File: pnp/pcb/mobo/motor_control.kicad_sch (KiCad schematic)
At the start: 0 parts

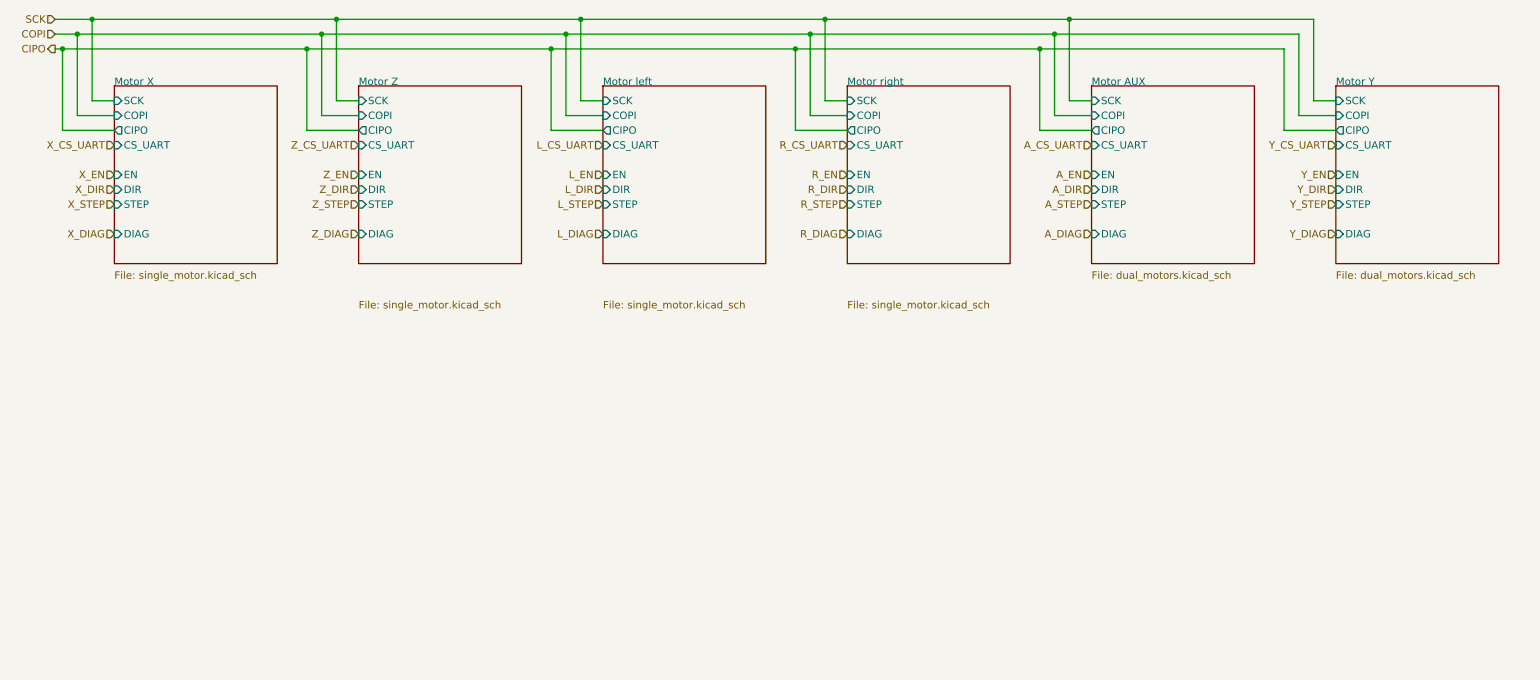
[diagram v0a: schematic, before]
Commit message: Update dual_motors.kicad_sch, mobo.kicad_pcb, mobo.kicad_pro, and 2 more files
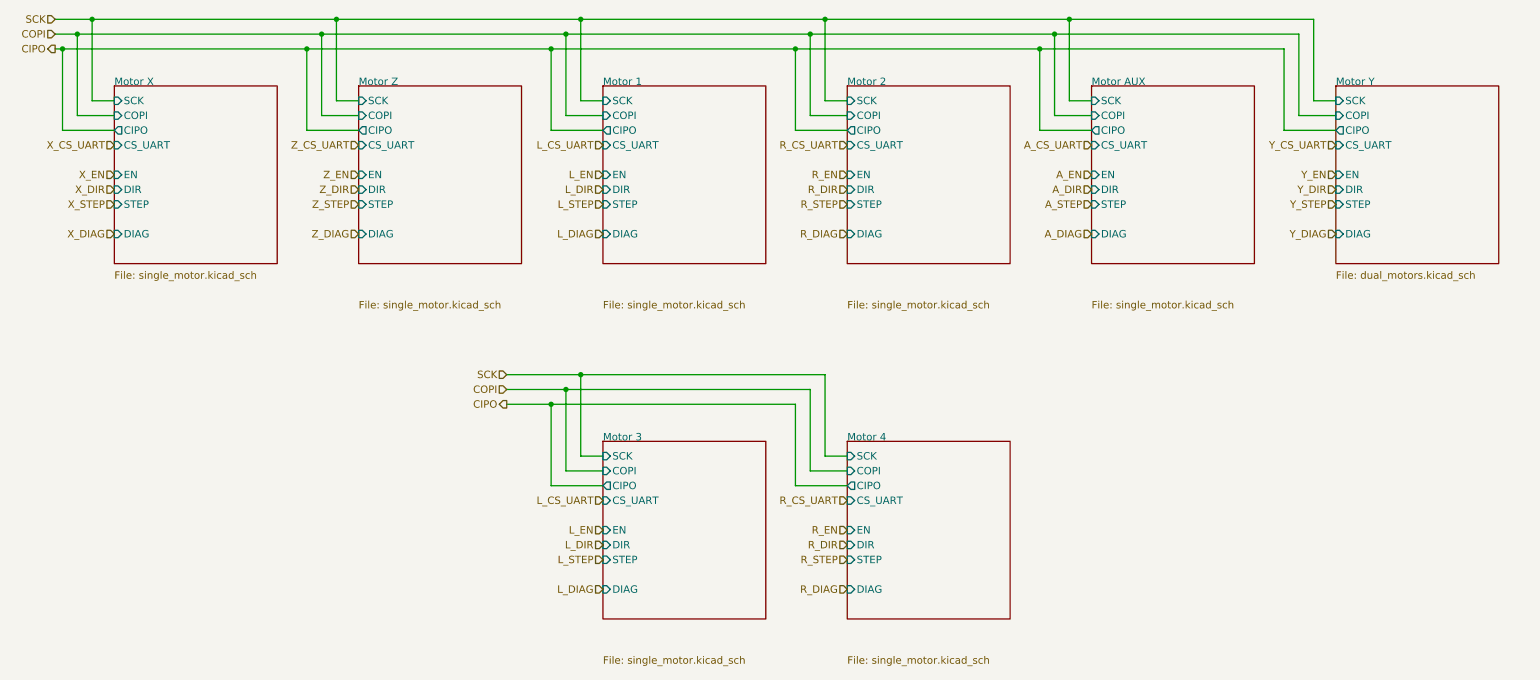
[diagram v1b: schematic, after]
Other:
- sheet Motor left renamed Motor 1
- sheet Motor right renamed Motor 2
- added sheet Motor 3 (single_motor.kicad_sch)
- added sheet Motor 4 (single_motor.kicad_sch)
- sheet Motor AUX: file dual_motors.kicad_sch -> single_motor.kicad_sch
